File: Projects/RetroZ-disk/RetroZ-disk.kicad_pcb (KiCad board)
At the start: 2 copper layers, 21 parts, among them IC1 CD74HC4050E, J1 Micro_SD_Card, J2 IO SELECTOR, U1 UA78M33CDCYR, U2 74LS138, U3 ATMEGA328P-PU, U4 7402, Y1 20Mhz

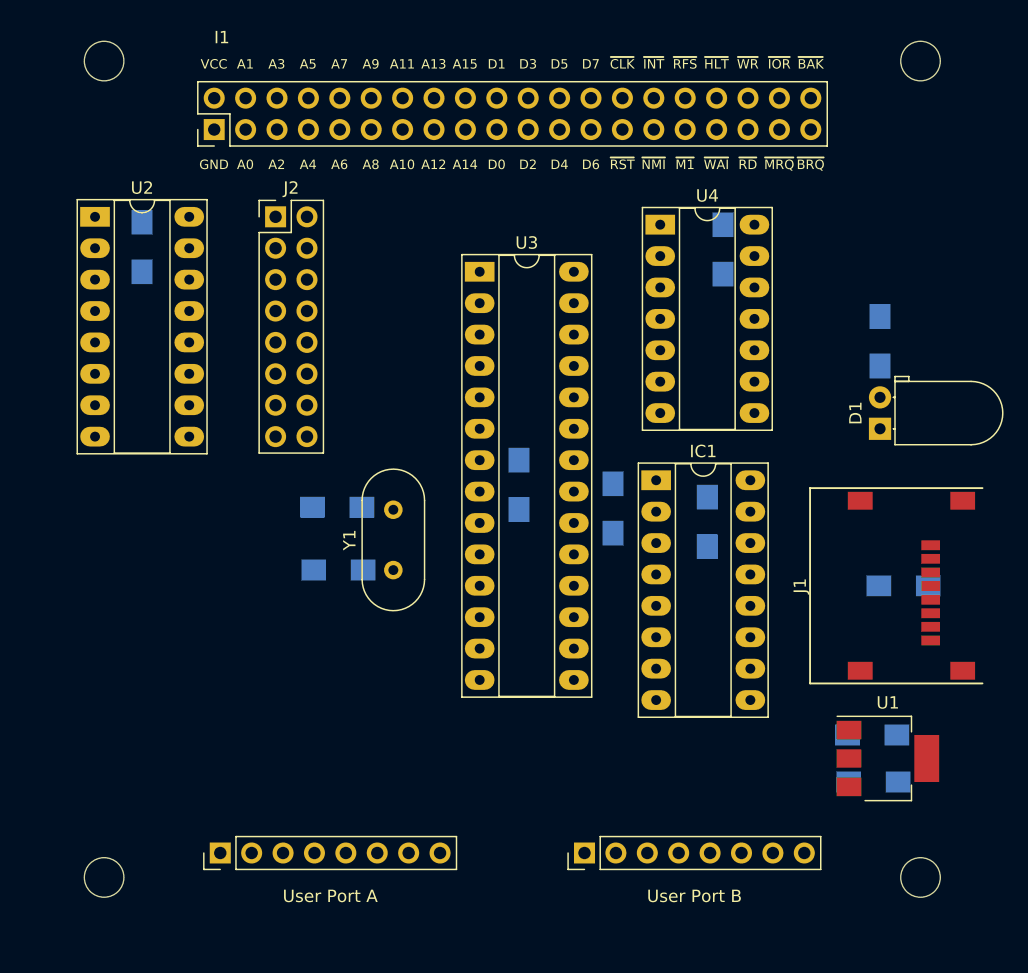
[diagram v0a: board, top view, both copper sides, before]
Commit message: RetroZ disk design done
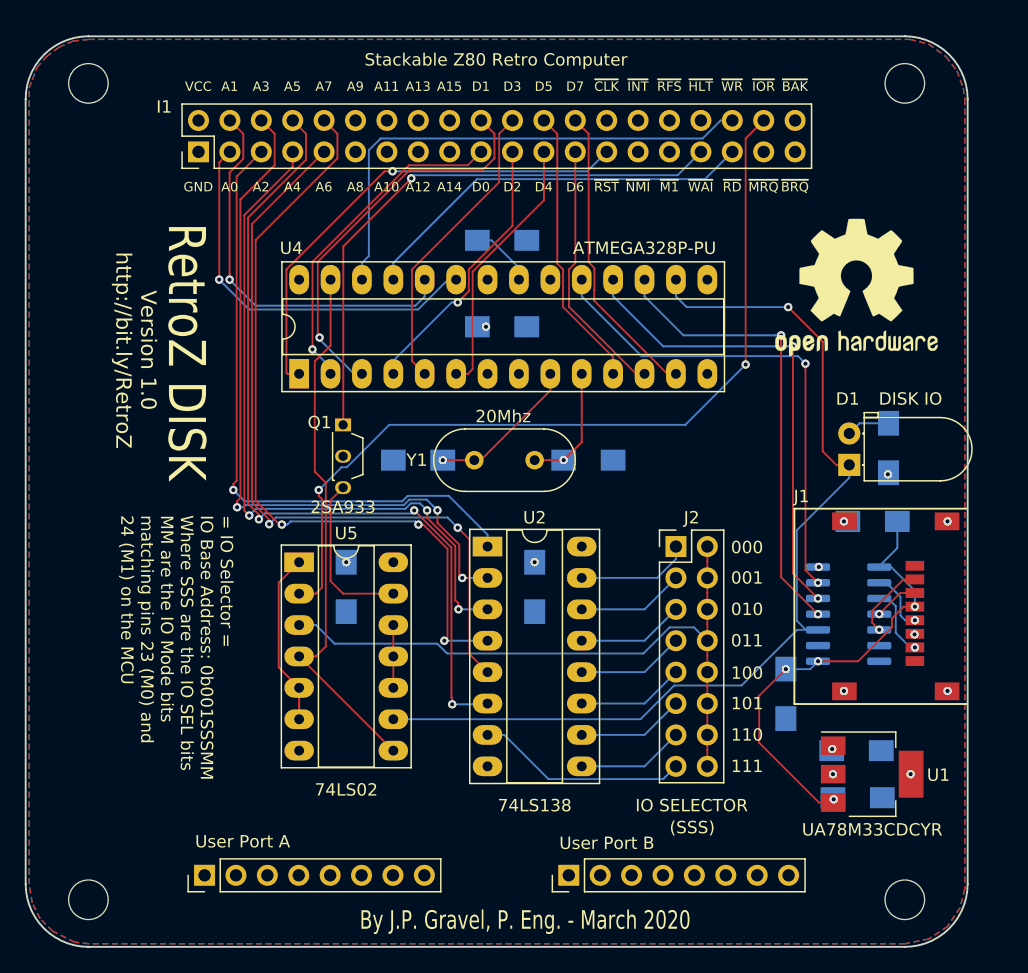
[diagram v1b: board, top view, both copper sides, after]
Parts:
- removed IC1: CD74HC4050E, Housings_DIP:DIP-16_W7.62mm_Socket_LongPads
- added Q1: 2SA933, Package_TO_SOT_THT:TO-92S_Wide, F.Cu at (137.5, 94.9)
- added REF**: OSHW-Logo2_14.6x12mm_SilkScreen, Symbol:OSHW-Logo2_14.6x12mm_SilkScreen, F.Cu at (179.1, 83.8)
- added U5: 74LS02, Housings_DIP:DIP-14_W7.62mm_Socket_LongPads, F.Cu at (134.0, 106.0)
- I1: value S80_Interface -> Stackable Z80 Retro Computer
- R2: value 150 -> 220
- U3: value ATMEGA328P-PU -> TXB0104DW; footprint Housings_DIP:DIP-28_W7.62mm_Socket_LongPads -> Package_SO:SOIC-14_3.9x8.7mm_P1.27mm; moved to B.Cu
- U4: value 7402 -> ATMEGA328P-PU; footprint Housings_DIP:DIP-14_W7.62mm_Socket_LongPads -> Housings_DIP:DIP-28_W7.62mm_Socket_LongPads
- moved C9 42.0 mm to (153.0, 108.0)
- moved J2 42.0 mm to (164.5, 104.8)
- moved U2 41.5 mm to (149.2, 104.8)
- moved C8 40.9 mm to (137.8, 108.0)
- moved U3 40.7 mm to (178.4, 110.2), turned to 180 degrees
- moved U4 31.6 mm to (134.0, 90.8), turned to 90 degrees
- moved R1 23.5 mm to (150.4, 80.0), turned to 0 degrees
- moved C4 22.1 mm to (157.4, 97.8), turned to 0 degrees
- moved Y1 14.5 mm to (153.0, 97.8), turned to 180 degrees
- moved C6 13.4 mm to (180.4, 102.7), turned to 180 degrees
- moved C5 12.9 mm to (173.4, 116.7), turned to 270 degrees
- moved C7 12.9 mm to (150.4, 87.0), turned to 0 degrees
- moved R2 8.66 mm to (181.7, 96.8), turned to 90 degrees
- moved C3 7.57 mm to (143.6, 97.8)
- moved D1 3.84 mm to (178.5, 98.2)
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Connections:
- J1 pad 2: Net-(IC1-Pad10) -> Net-(J1-Pad2)
- J1 pad 3: Net-(IC1-Pad6) -> Net-(J1-Pad3)
- J1 pad 5: Net-(IC1-Pad2) -> Net-(J1-Pad5)
- J1 pad 7: Net-(IC1-Pad5) -> Net-(J1-Pad7)
- U3 pad 1: /~RESET -> VDD
- U3 pad 10: Net-(C4-Pad1) -> /~SS
- U3 pad 11: /D5 -> /MOSI
- U3 pad 12: /D6 -> /MISO
- U3 pad 13: /D7 -> /SCK
- U3 pad 14: Net-(U3-Pad14) -> VCC
- U3 pad 2: /D0 -> Net-(J1-Pad5)
- U3 pad 3: /D1 -> Net-(J1-Pad7)
- U3 pad 4: /D2 -> Net-(J1-Pad3)
- U3 pad 5: /D3 -> Net-(J1-Pad2)
- U3 pad 6: /D4 -> Net-(U3-Pad6)
- U3 pad 7: VCC -> GND
- U3 pad 8: GND -> VDD
- U3 pad 9: Net-(C3-Pad1) -> Net-(U3-Pad9)
- U4 pad 1: Net-(U4-Pad1) -> /~RESET
- U4 pad 10: (no net) -> Net-(C4-Pad1)
- U4 pad 11: (no net) -> /D5
- U4 pad 12: (no net) -> /D6
- U4 pad 13: (no net) -> /D7
- U4 pad 14: (no net) -> Net-(U4-Pad14)
- U4 pad 2: /~IORQ -> /D0
- U4 pad 3: /~SEL -> /D1
- U4 pad 4: /~CS -> /D2
- U4 pad 5: Net-(U4-Pad1) -> /D3
- U4 pad 6: Net-(U4-Pad1) -> /D4
- U4 pad 7: (no net) -> VCC
- U4 pad 8: (no net) -> GND
- U4 pad 9: (no net) -> Net-(C3-Pad1)
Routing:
- net /~SS: track 0.00 -> 79.0 mm, vias 0 -> 1
- net /~IORQ: track 0.00 -> 69.1 mm, vias 0 -> 2
- net Net-(I1-Pad8): track 0.00 -> 67.8 mm, vias 0 -> 3
- net Net-(I1-Pad10): track 0.00 -> 62.3 mm, vias 0 -> 3
- net Net-(I1-Pad9): track 0.00 -> 61.6 mm, vias 0 -> 2
- net Net-(I1-Pad6): track 0.00 -> 58.6 mm, vias 0 -> 3
- net Net-(I1-Pad7): track 0.00 -> 57.6 mm, vias 0 -> 3
- net /~SEL: track 0.00 -> 53.1 mm
- net Net-(I1-Pad5): track 0.00 -> 51.7 mm, vias 0 -> 1
- net /~WAIT: track 0.00 -> 46.5 mm, vias 0 -> 1
- net /~CS: track 0.00 -> 43.8 mm
- net /~WR: track 0.00 -> 41.1 mm
- net /SCK: track 0.00 -> 39.9 mm, vias 0 -> 2
- net /~RESET: track 0.00 -> 39.3 mm, vias 0 -> 1
- net /MISO: track 0.00 -> 38.8 mm, vias 0 -> 2
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- added copper zone on B.Cu, net GND
- added copper zone on F.Cu, net VCC
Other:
- board outline added: 76.2 x 73.7 mm
- net class Default: clearance 0.2 -> 0.1524; trace_width 0.25 -> 0.1524; via_dia 0.8 -> 0.6858; via_drill 0.4 -> 0.3302
- rule trace_clearance: 0.2 -> 0.1524
- rule trace_min: 0.2 -> 0.1524
- rule via_min_drill: 0.3 -> 0.3302
- rule via_min_size: 0.4 -> 0.6858
- board text added: "(SSS)"
- board text added: "000"
- board text added: "001"
- board text added: "010"
- board text added: "011"
- board text added: "100"
- board text added: "101"
- board text added: "110"
- board text added: "111"
- board text added: "= IO Selector = IO Base Address: 0b001SSSMM Where SSS are the IO SEL bits MM are the IO Mode bits matching pins 23 (M0) and 24 (M1) on the MCU"
- board text added: "By J.P. Gravel, P. Eng. - March 2020"
- board text added: "RetroZ DISK"
- board text added: "Stackable Z80 Retro Computer"
- board text added: "Version 1.0 http://bit.ly/RetroZ"

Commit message: added interrupt signal
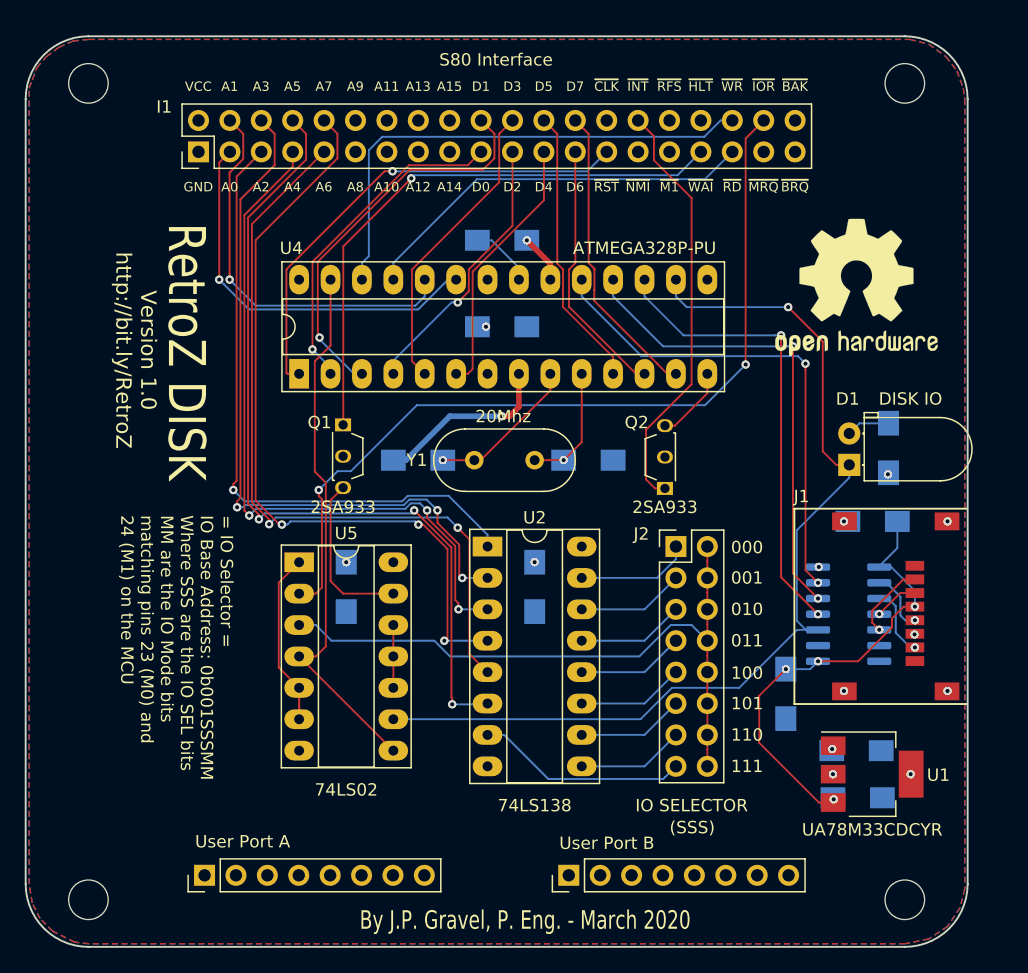
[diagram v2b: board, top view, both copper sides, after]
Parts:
- added Q2: 2SA933, Package_TO_SOT_THT:TO-92S_Wide, F.Cu at (163.6, 100.1)
- I1: value Stackable Z80 Retro Computer -> S80 Interface
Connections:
- I1 pad 30: Net-(I1-Pad30) -> /~INT
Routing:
- net /~INT: track 0.00 -> 34.2 mm
- net GND: track 0.00 -> 14.6 mm, vias 7 -> 8
- net Net-(Q2-Pad3): track 0.00 -> 6.08 mm
- net VCC: track 0.00 -> 3.96 mm, vias 6 -> 7

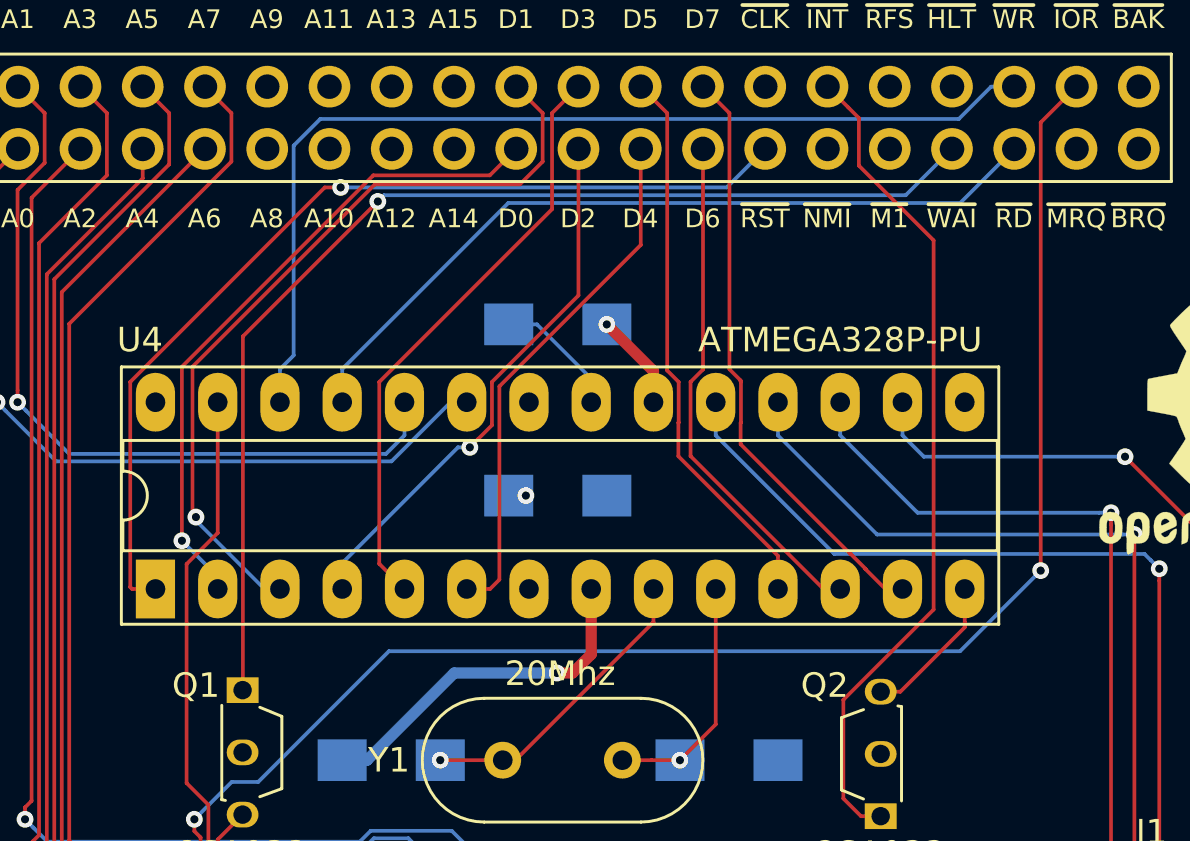
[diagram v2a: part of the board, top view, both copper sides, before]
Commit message: fixed interrupt ack processing
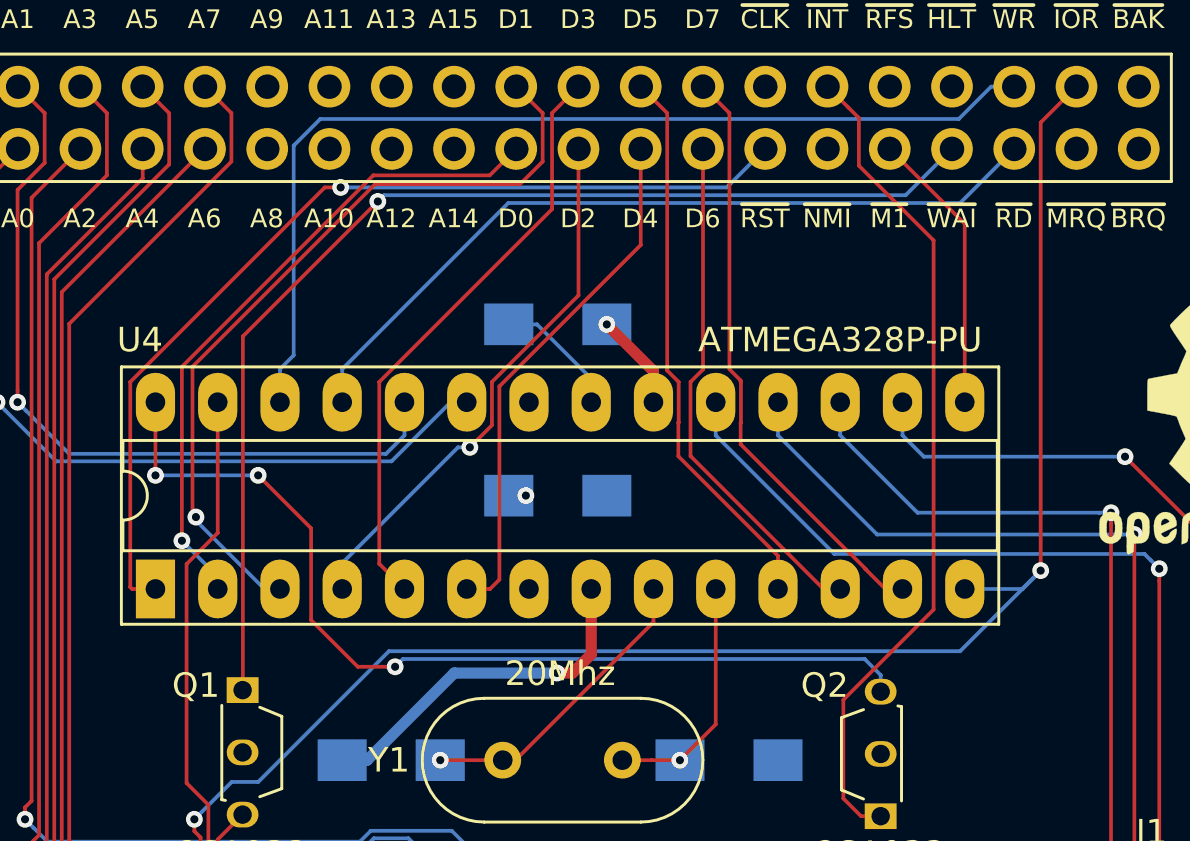
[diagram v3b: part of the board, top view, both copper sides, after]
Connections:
- I1 pad 31: Net-(I1-Pad31) -> /~M1
- U4 pad 14: Net-(Q2-Pad3) -> /~IORQ
- U4 pad 15: Net-(U4-Pad15) -> /~M1
- U4 pad 28: Net-(U4-Pad28) -> Net-(Q2-Pad3)
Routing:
- net Net-(Q2-Pad3): track 6.08 -> 39.1 mm, vias 0 -> 3
- net /~M1: track 0.00 -> 11.6 mm
- net /~IORQ: track 69.1 -> 72.5 mm

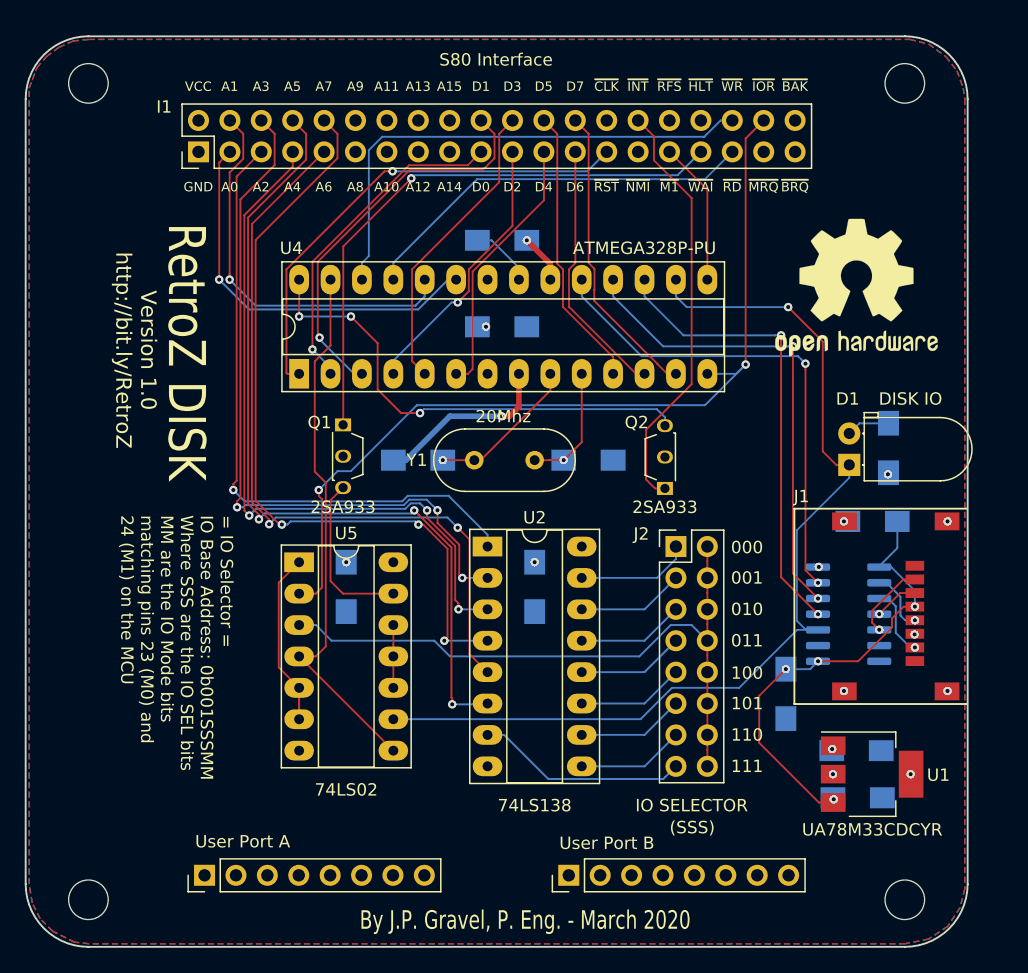
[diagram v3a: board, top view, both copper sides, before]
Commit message: removed interrupt management, added arduino code
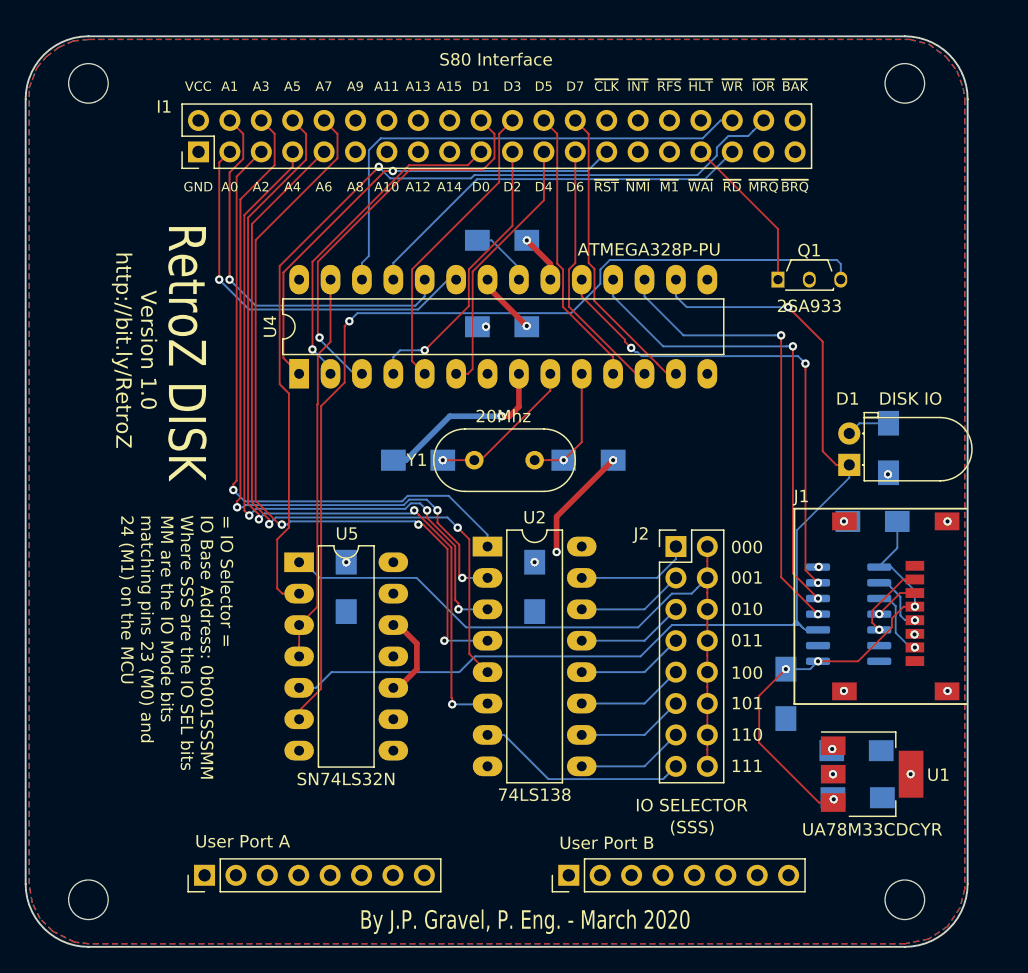
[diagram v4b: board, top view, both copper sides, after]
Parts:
- removed Q2: 2SA933, Package_TO_SOT_THT:TO-92S_Wide
- removed REF**: OSHW-Logo2_14.6x12mm_SilkScreen, Symbol:OSHW-Logo2_14.6x12mm_SilkScreen
- U2: footprint Housings_DIP:DIP-16_W7.62mm_Socket_LongPads -> Package_DIP:DIP-16_W7.62mm_LongPads
- U4: footprint Housings_DIP:DIP-28_W7.62mm_Socket_LongPads -> Package_DIP:DIP-28_W7.62mm_LongPads
- U5: value 74LS02 -> SN74LS32N; footprint Housings_DIP:DIP-14_W7.62mm_Socket_LongPads -> Package_DIP:DIP-14_W7.62mm_LongPads
- moved Q1 37.1 mm to (172.7, 83.2), turned to 0 degrees
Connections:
- U4 pad 14: /~IORQ -> Net-(U4-Pad14)
- U4 pad 15: /~M1 -> Net-(U4-Pad15)
- U5 pad 1: Net-(U5-Pad1) -> /~SEL
- U5 pad 10: Net-(U5-Pad10) -> GND
- U5 pad 11: Net-(U5-Pad10) -> Net-(U5-Pad11)
- U5 pad 12: Net-(U5-Pad10) -> GND
- U5 pad 13: Net-(Q1-Pad3) -> GND
- U5 pad 3: /~SEL -> /~CS
- U5 pad 5: Net-(U5-Pad1) -> /~SS
- U5 pad 6: Net-(U5-Pad1) -> Net-(Q1-Pad3)
- U5 pad 8: /~CS -> Net-(U5-Pad8)
- U5 pad 9: /~SS -> GND
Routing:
- net Net-(Q1-Pad3): track 13.5 -> 77.8 mm, vias 0 -> 1
- net Net-(U4-Pad28): track 39.1 -> 0.00 mm, vias 3 -> 0
- net /~INT: track 34.2 -> 0.00 mm
- net /~WAIT: track 46.5 -> 12.9 mm, vias 1 -> 0
- net GND: track 14.6 -> 36.2 mm, vias 8 -> 11
- net Net-(U5-Pad1): track 16.6 -> 0.00 mm
- net /~CS: track 43.8 -> 31.5 mm
- net /~M1: track 11.6 -> 0.00 mm
- net /~SS: track 79.0 -> 86.8 mm
- net Net-(U5-Pad10): track 5.08 -> 0.00 mm
- net /~IORQ: track 72.5 -> 73.9 mm, vias 2 -> 1
- net /~SEL: track 53.4 -> 54.6 mm
- net /D2: track 22.2 -> 23.1 mm
- net /SCK: track 39.9 -> 40.0 mm, vias 2 -> 3
